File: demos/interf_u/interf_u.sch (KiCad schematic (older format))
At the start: 24 parts, among them P1 DB25FEMELLE, U1 74LS245, U2 74LS688, U3 74LS541, U5 628128, U8 EP600, U9 4003APG120, X1 8MHz

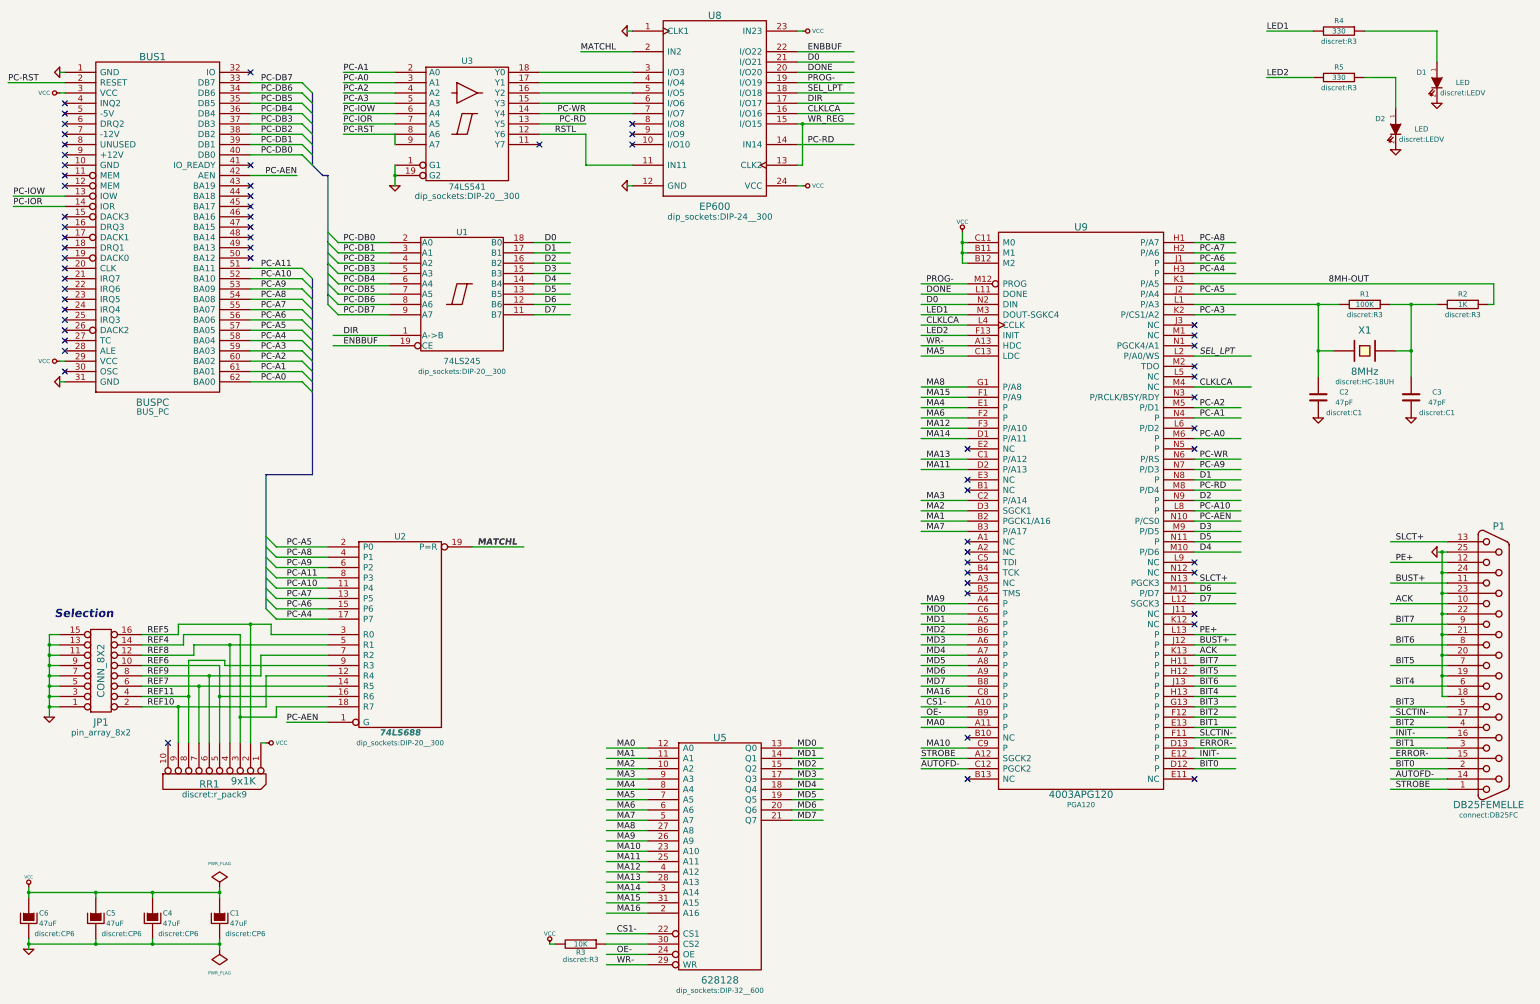
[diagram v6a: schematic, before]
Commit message: Pcbnew and Gerbview: layer manager: use double click to edit color (as usual to edit someting) and simple click (as previously) to select the layer. Reason: avoid opening the color dialog each time a new layer is selected. Update interf_u demo to use recent library components..
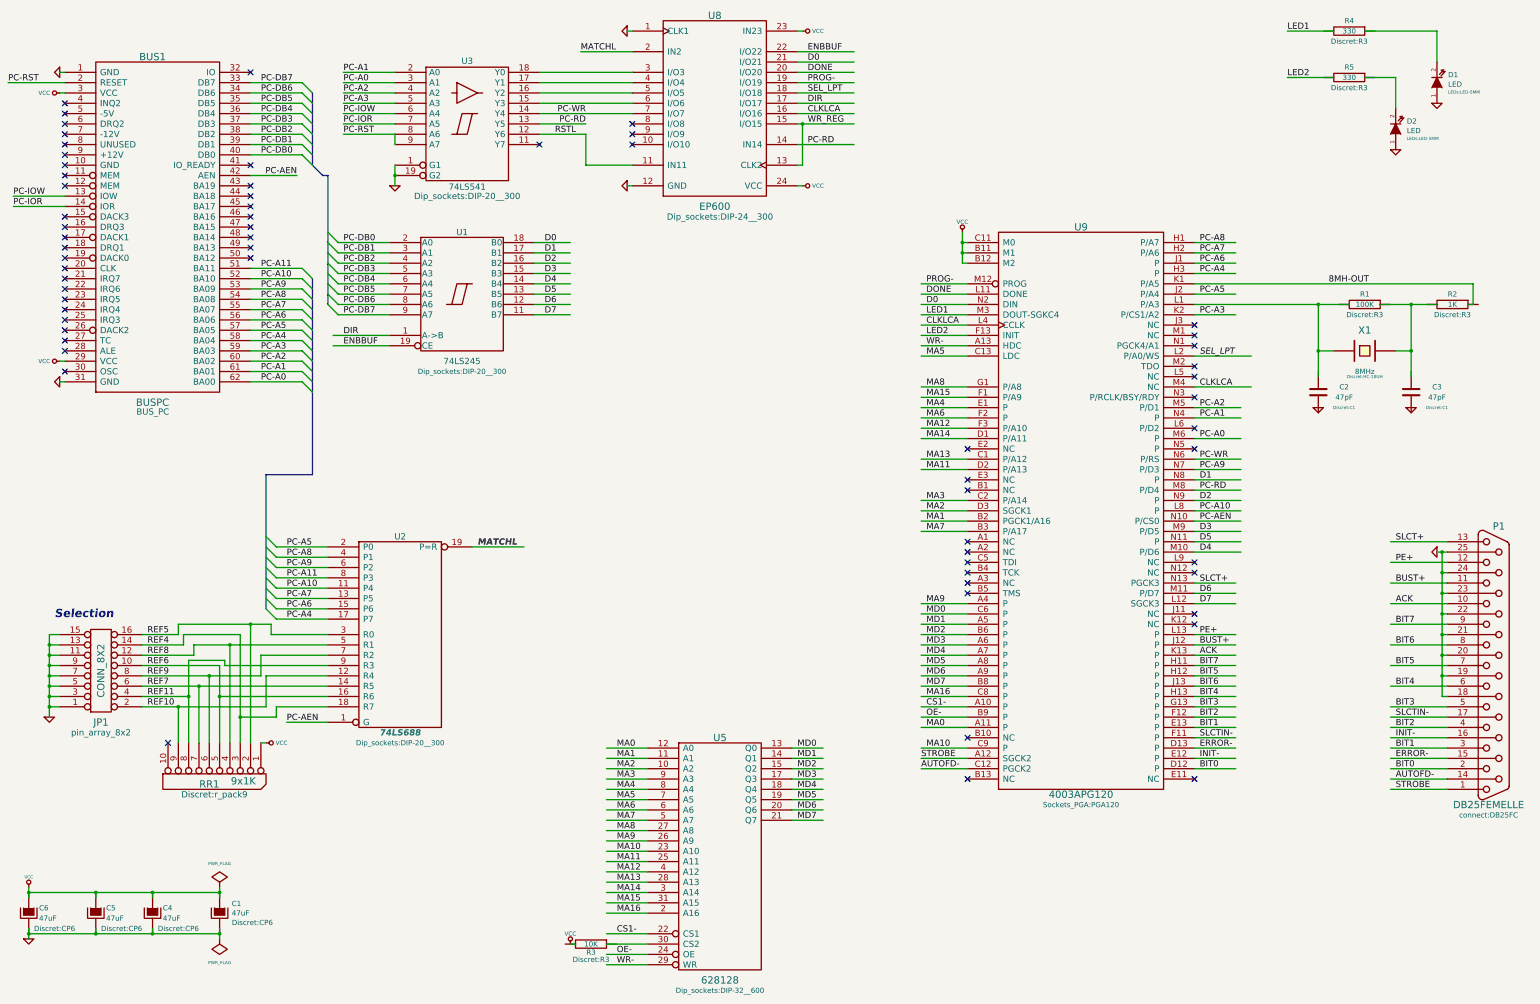
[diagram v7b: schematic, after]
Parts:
- C1, C4, C5, C6: footprint discret:CP6 -> Discret:CP6
- C2, C3: footprint discret:C1 -> Discret:C1
- D1, D2: footprint discret:LEDV -> LEDs:LED-5MM
- R1, R2, R3, R4, R5: footprint discret:R3 -> Discret:R3
- RR1: footprint discret:r_pack9 -> Discret:r_pack9
- U1, U2, U3: footprint dip_sockets:DIP-20__300 -> Dip_sockets:DIP-20__300
- U5: footprint dip_sockets:DIP-32__600 -> Dip_sockets:DIP-32__600
- U8: footprint dip_sockets:DIP-24__300 -> Dip_sockets:DIP-24__300
- U9: footprint PGA120 -> Sockets_PGA:PGA120
- X1: footprint discret:HC-18UH -> Discret:HC-18UH
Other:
- moved on the sheet: C1, C2, C3, C4, C5, C6, R2, R3, R4, R5
